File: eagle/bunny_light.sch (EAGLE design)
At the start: 16 parts, among them IC1 ATMEGA328P_PDIP, J1 USB-B-S, U1 5V, Y1 16Mhz

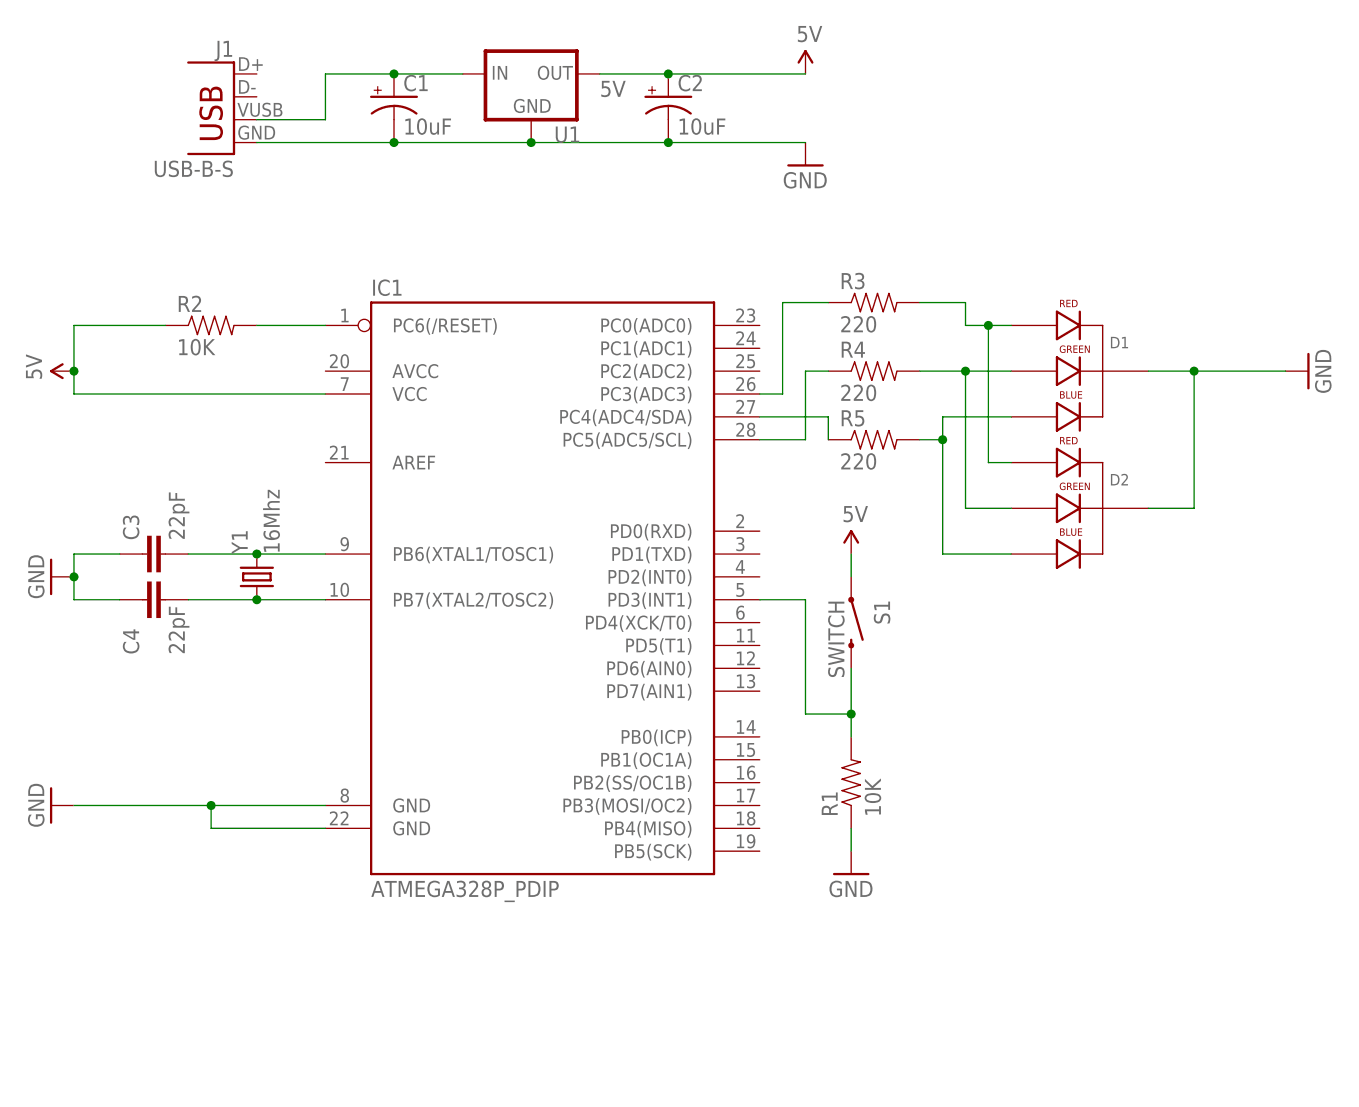
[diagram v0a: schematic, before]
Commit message: Second iteration after receiving the board: 	- corrected wrong components (surface mount vs. through hole) 	- added PTC fuse 	- used larger footprints for the resistors 	- corrected RGB LEDs overlapping
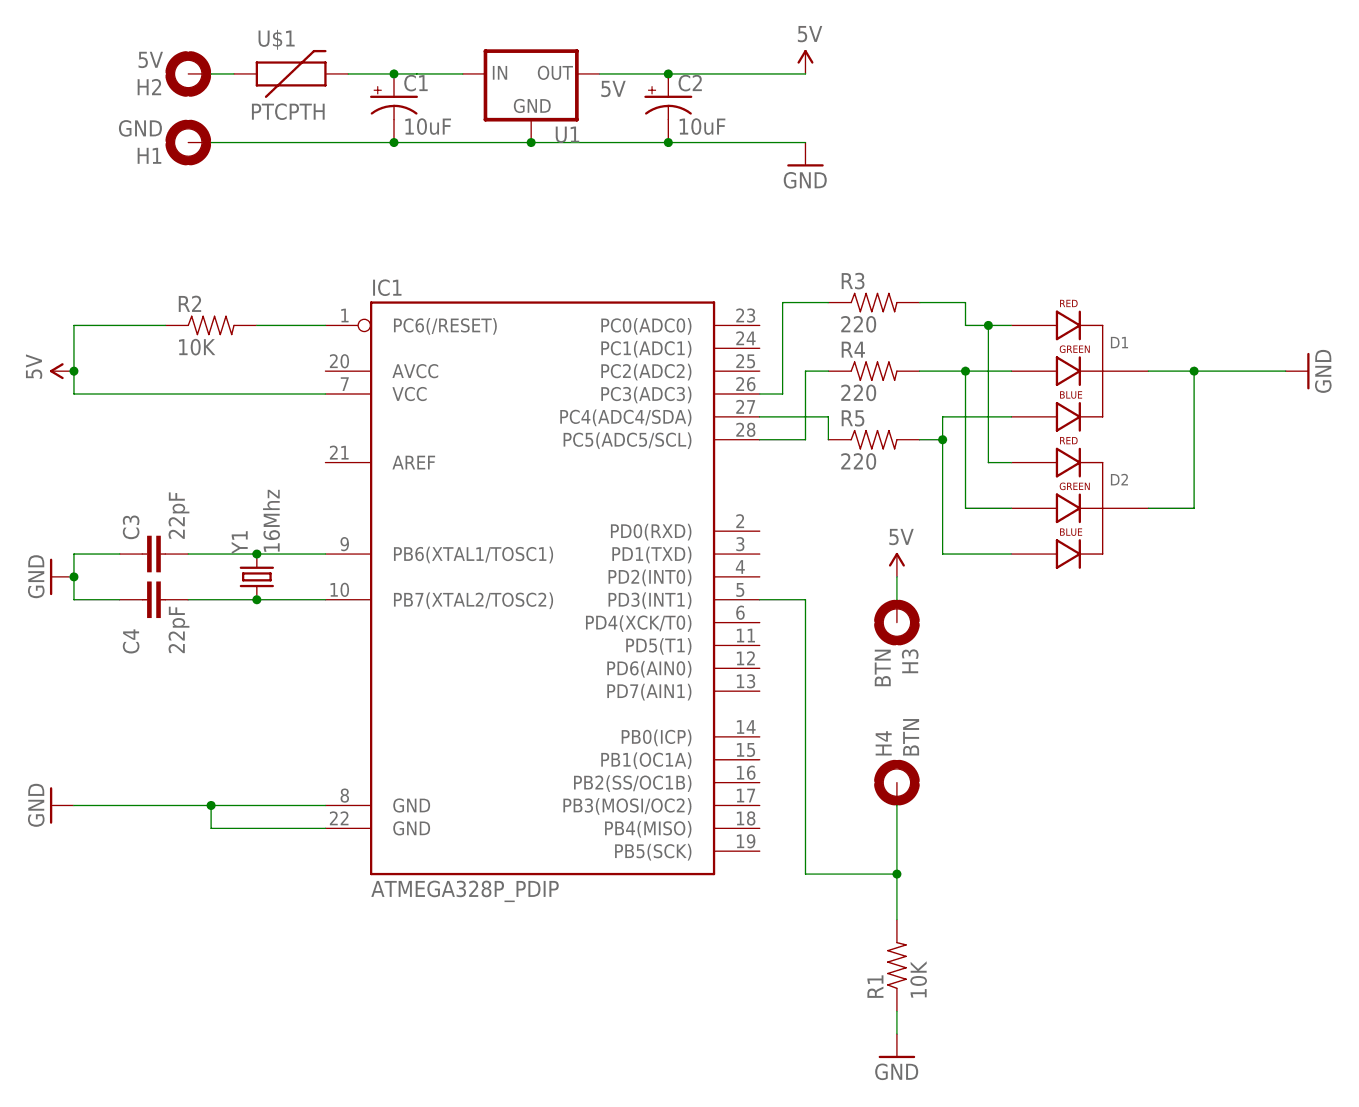
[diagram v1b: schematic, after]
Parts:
- removed J1: USB-B-S, SparkFun-Connectors:USB-B-S
- removed S1: SWITCH, SparkFun-Electromechanical:SWITCH-MOMENTARY-2PTH_REED2
- added H1: GND, holes:MOUNT-PAD-ROUND2.8
- added H2: 5V, holes:MOUNT-PAD-ROUND2.8
- added H3, H4: BTN, holes:MOUNT-PAD-ROUND2.8
- added U$1: PTCPTH, SparkFun-PowerIC:PTCPTH
- C1, C2: device SparkFun-Capacitors:CAP_POL1206 -> SparkFun-Capacitors:CAP_POLPTH1
- R1, R2, R3, R4, R5: device SparkFun-Resistors:RESISTORPTH-1/6W -> SparkFun-Resistors:RESISTOREZ
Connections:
- new net N$12: H2.MOUNT, U$1.1
- net 5V: now also H3.MOUNT; no longer S1.1
- net GND: now also H1.MOUNT; no longer J1.GND
- net N$1: now also U$1.2; no longer J1.VBUS
- net N$5: now also H4.MOUNT; no longer S1.2
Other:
- moved on the sheet: R1
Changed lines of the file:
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@@
 <attributes>
 <attribute name="CNAME" value="Arduino Bunny Nightlight"/>
-<attribute name="CREVISION" value="1.0"/>
+<attribute name="CREVISION" value="1.1"/>
 <attribute name="DESIGNER" value="Nikita Pchelin"/>
 </attributes>
@@
 <parts>
 <part name="IC1" library="SparkFun-DigitalIC" deviceset="ATMEGA328P_PDIP" device=""/>
-<part name="J1" library="SparkFun-Connectors" deviceset="USB" device="-B-S"/>
-<part name="C2" library="SparkFun-Capacitors" deviceset="CAP_POL" device="1206" value="10uF"/>
-<part name="C1" library="SparkFun-Capacitors" deviceset="CAP_POL" device="1206" value="10uF"/>
+<part name="C2" library="SparkFun-Capacitors" deviceset="CAP_POL" device="PTH1" value="10uF"/>
+<part name="C1" library="SparkFun-Capacitors" deviceset="CAP_POL" device="PTH1" value="10uF"/>
 <part name="U1" library="SparkFun-PowerIC" deviceset="V_REG_78XX" device="SIDE" value="5V"/>
-<part name="R1" library="SparkFun-Resistors" deviceset="RESISTOR" device="PTH-1/6W" value="10K"/>
-<part name="R2" library="SparkFun-Resistors" deviceset="RESISTOR" device="PTH-1/6W" value="10K"/>
-<part name="R3" library="SparkFun-Resistors" deviceset="RESISTOR" device="PTH-1/6W" value="220"/>
-<part name="R4" library="SparkFun-Resistors" deviceset="RESISTOR" device="PTH-1/6W" value="220"/>
-<part name="R5" library="SparkFun-Resistors" deviceset="RESISTOR" device="PTH-1/6W" value="220"/>
+<part name="R1" library="SparkFun-Resistors" deviceset="RESISTOR" device="EZ" value="10K"/>
+<part name="R2" library="SparkFun-Resistors" deviceset="RESISTOR" device="EZ" value="10K"/>
+<part name="R3" library="SparkFun-Resistors" deviceset="RESISTOR" device="EZ" value="220"/>
+<part name="R4" library="SparkFun-Resistors" deviceset="RESISTOR" device="EZ" value="220"/>
+<part name="R5" library="SparkFun-Resistors" deviceset="RESISTOR" device="EZ" value="220"/>
 <part name="Y1" library="SparkFun-FreqCtrl" deviceset="CRYSTAL" device="HC49US" value="16Mhz"/>
 <part name="C3" library="SparkFun-Passives" deviceset="CAP" device="_" value="22pF"/>
 <part name="C4" library="SparkFun-Passives" deviceset="CAP" device="_" value="22pF"/>
-<part name="S1" library="SparkFun-Electromechanical" deviceset="SWITCH-MOMENTARY-2" device="PTH_REED2" value="SWITCH"/>
 <part name="GND1" library="SparkFun-Aesthetics" deviceset="GND" device=""/>
 <part name="GND2" library="SparkFun-Aesthetics" deviceset="GND" device=""/>
@@
 <part name="GND6" library="SparkFun-Aesthetics" deviceset="GND" device=""/>
 <part name="FRAME1" library="SparkFun-Aesthetics" deviceset="FRAME-A4L" device=""/>
+<part name="U$1" library="SparkFun-PowerIC" deviceset="PTC" device="PTH"/>
+<part name="H1" library="holes" deviceset="MOUNT-PAD-ROUND" device="2.8" value="GND"/>
+<part name="H2" library="holes" deviceset="MOUNT-PAD-ROUND" device="2.8" value="5V"/>
+<part name="H3" library="holes" deviceset="MOUNT-PAD-ROUND" device="2.8" value="BTN"/>
+<part name="H4" library="holes" deviceset="MOUNT-PAD-ROUND" device="2.8" value="BTN"/>
 </parts>
 <sheets>
@@
 <instances>
 <instance part="IC1" gate="G$1" x="558.8" y="10.16"/>
-<instance part="J1" gate="G$1" x="525.78" y="55.88" rot="MR0"/>
 <instance part="C2" gate="G$1" x="574.04" y="60.96"/>
 <instance part="C1" gate="G$1" x="543.56" y="60.96"/>
@@
 <attribute name="VALUE" x="566.42" y="60.96" size="1.778" layer="96"/>
 </instance>
-<instance part="R1" gate="G$1" x="594.36" y="-15.24" rot="R90"/>
+<instance part="R1" gate="G$1" x="599.44" y="-35.56" rot="R90"/>
 <instance part="R2" gate="G$1" x="523.24" y="35.56"/>
 <instance part="R3" gate="G$1" x="596.9" y="38.1"/>
@@
 <attribute name="VALUE" x="520.319" y="-1.016" size="1.778" layer="96" rot="R90"/>
 </instance>
-<instance part="S1" gate="G$1" x="594.36" y="2.54" smashed="yes" rot="R270">
-<attribute name="NAME" x="596.9" y="5.08" size="1.778" layer="95" rot="R270"/>
-<attribute name="VALUE" x="591.82" y="5.08" size="1.778" layer="96" rot="R270"/>
-</instance>
 <instance part="GND1" gate="1" x="505.46" y="7.62" rot="R270"/>
 <instance part="GND2" gate="1" x="505.46" y="-17.78" rot="R270"/>
-<instance part="GND4" gate="1" x="594.36" y="-25.4"/>
+<instance part="GND4" gate="1" x="599.44" y="-45.72"/>
 <instance part="GND5" gate="1" x="589.28" y="53.34"/>
 <instance part="USB" gate="G$1" x="589.28" y="63.5"/>
 <instance part="SUPPLY4" gate="G$1" x="508" y="30.48" rot="R90"/>
-<instance part="SUPPLY1" gate="G$1" x="594.36" y="10.16"/>
+<instance part="SUPPLY1" gate="G$1" x="599.44" y="7.62"/>
 <instance part="D1" gate="G$1" x="617.22" y="30.48"/>
 <instance part="D2" gate="G$1" x="617.22" y="15.24"/>
 <instance part="GND6" gate="1" x="645.16" y="30.48" rot="R90"/>
 <instance part="FRAME1" gate="G$1" x="426.72" y="-66.04"/>
+<instance part="U$1" gate="G$1" x="530.86" y="63.5"/>
+<instance part="H1" gate="G$1" x="520.7" y="55.88" smashed="yes" rot="R180">
+<attribute name="NAME" x="517.906" y="55.2958" size="1.778" layer="95" rot="R180"/>
+<attribute name="VALUE" x="517.906" y="58.3438" size="1.778" layer="96" rot="R180"/>
+</instance>
+<instance part="H2" gate="G$1" x="520.7" y="63.5" smashed="yes" rot="R180">
+<attribute name="NAME" x="517.906" y="62.9158" size="1.778" layer="95" rot="R180"/>
+<attribute name="VALUE" x="517.906" y="65.9638" size="1.778" layer="96" rot="R180"/>
+</instance>
+<instance part="H3" gate="G$1" x="599.44" y="2.54" smashed="yes" rot="R270">
+<attribute name="NAME" x="600.0242" y="-0.254" size="1.778" layer="95" rot="R270"/>
+<attribute name="VALUE" x="596.9762" y="-0.254" size="1.778" layer="96" rot="R270"/>
+</instance>
+<instance part="H4" gate="G$1" x="599.44" y="-15.24" smashed="yes" rot="R90">
+<attribute name="NAME" x="598.8558" y="-12.446" size="1.778" layer="95" rot="R90"/>
+<attribute name="VALUE" x="601.9038" y="-12.446" size="1.778" layer="96" rot="R90"/>
+</instance>
 </instances>
 <busses>
@@
 <net name="N$1" class="0">
 <segment>
-<pinref part="J1" gate="G$1" pin="VBUS"/>
-<wire x1="528.32" y1="58.42" x2="535.94" y2="58.42" width="0.1524" layer="91"/>
-<wire x1="535.94" y1="58.42" x2="535.94" y2="63.5" width="0.1524" layer="91"/>
 <pinref part="C1" gate="G$1" pin="+"/>
-<wire x1="535.94" y1="63.5" x2="543.56" y2="63.5" width="0.1524" layer="91"/>
 <pinref part="U1" gate="G$1" pin="IN"/>
-<wire x1="543.56" y1="63.5" x2="551.18" y2="63.5" width="0.1524" layer="91"/>
+<wire x1="543.56" y1="63.5" x2="546.1" y2="63.5" width="0.1524" layer="91"/>
+<pinref part="U$1" gate="G$1" pin="2"/>
+<wire x1="546.1" y1="63.5" x2="551.18" y2="63.5" width="0.1524" layer="91"/>
+<wire x1="538.48" y1="63.5" x2="543.56" y2="63.5" width="0.1524" layer="91"/>
 <junction x="543.56" y="63.5"/>
 </segment>
@@
 </segment>
 <segment>
-<pinref part="S1" gate="G$1" pin="1"/>
 <pinref part="SUPPLY1" gate="G$1" pin="5V"/>
-<wire x1="594.36" y1="7.62" x2="594.36" y2="10.16" width="0.1524" layer="91"/>
+<wire x1="599.44" y1="5.08" x2="599.44" y2="7.62" width="0.1524" layer="91"/>
+<pinref part="H3" gate="G$1" pin="MOUNT"/>
 </segment>
 </net>
 <net name="GND" class="0">
 <segment>
-<pinref part="J1" gate="G$1" pin="GND"/>
 <pinref part="C1" gate="G$1" pin="-"/>
-<wire x1="528.32" y1="55.88" x2="543.56" y2="55.88" width="0.1524" layer="91"/>
+<wire x1="523.24" y1="55.88" x2="543.56" y2="55.88" width="0.1524" layer="91"/>
 <pinref part="U1" gate="G$1" pin="GND"/>
 <wire x1="543.56" y1="55.88" x2="558.8" y2="55.88" width="0.1524" layer="91"/>
@@
 <wire x1="574.04" y1="55.88" x2="589.28" y2="55.88" width="0.1524" layer="91"/>
 <junction x="574.04" y="55.88"/>
+<pinref part="H1" gate="G$1" pin="MOUNT"/>
 </segment>
 <segment>
@@
 <pinref part="GND4" gate="1" pin="GND"/>
 <pinref part="R1" gate="G$1" pin="1"/>
-<wire x1="594.36" y1="-22.86" x2="594.36" y2="-20.32" width="0.1524" layer="91"/>
+<wire x1="599.44" y1="-43.18" x2="599.44" y2="-40.64" width="0.1524" layer="91"/>
 </segment>
 <segment>
@@
 <segment>
 <pinref part="R1" gate="G$1" pin="2"/>
-<pinref part="S1" gate="G$1" pin="2"/>
-<wire x1="594.36" y1="-10.16" x2="594.36" y2="-7.62" width="0.1524" layer="91"/>
+<wire x1="599.44" y1="-30.48" x2="599.44" y2="-25.4" width="0.1524" layer="91"/>
 <pinref part="IC1" gate="G$1" pin="PD3(INT1)"/>
-<wire x1="594.36" y1="-7.62" x2="594.36" y2="-2.54" width="0.1524" layer="91"/>
+<wire x1="599.44" y1="-25.4" x2="599.44" y2="-17.78" width="0.1524" layer="91"/>
 <wire x1="584.2" y1="5.08" x2="589.28" y2="5.08" width="0.1524" layer="91"/>
-<wire x1="589.28" y1="5.08" x2="589.28" y2="-7.62" width="0.1524" layer="91"/>
-<wire x1="589.28" y1="-7.62" x2="594.36" y2="-7.62" width="0.1524" layer="91"/>
-<junction x="594.36" y="-7.62"/>
+<wire x1="589.28" y1="5.08" x2="589.28" y2="-25.4" width="0.1524" layer="91"/>
+<wire x1="589.28" y1="-25.4" x2="599.44" y2="-25.4" width="0.1524" layer="91"/>
+<junction x="599.44" y="-25.4"/>
+<pinref part="H4" gate="G$1" pin="MOUNT"/>
 </segment>
 </net>
@@
 </segment>
 </net>
+<net name="N$12" class="0">
+<segment>
+<pinref part="H2" gate="G$1" pin="MOUNT"/>
+<pinref part="U$1" gate="G$1" pin="1"/>
+<wire x1="523.24" y1="63.5" x2="525.78" y2="63.5" width="0.1524" layer="91"/>
+</segment>
+</net>
